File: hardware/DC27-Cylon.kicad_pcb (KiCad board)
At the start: 2 copper layers, 29 parts, among them U1 STM32F030K6Tx, U2 AZ1117-3.3, Y1 16MHz

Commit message: some fixes for fab
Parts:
- added BT1: >VALUE, Sparkfun_Connectors:1X02, F.Cu at (58.4, 63.5)
- C1, C2, C3, C4, C5: footprint Capacitors_SMD:C_0603 -> Sparkfun_Capacitors:0603
- U2: footprint Digikey:SOT-23-3 -> Package_TO_SOT_SMD:SOT-223-3_TabPin2
- moved D1 67.8 mm to (64.8, 78.7), turned to 270 degrees
- moved R1 65.5 mm to (64.8, 74.9), turned to 270 degrees
- moved D2 64.5 mm to (62.2, 78.7), turned to 270 degrees
- moved R2 60.8 mm to (62.2, 74.9), turned to 270 degrees
- moved D3 60.8 mm to (59.7, 78.7), turned to 270 degrees
- moved R4 60.3 mm to (57.1, 74.9), turned to 270 degrees
- moved R6 60.2 mm to (52.1, 74.9), turned to 270 degrees
- moved D7 59.0 mm to (49.5, 78.7), turned to 270 degrees
- moved D9 58.9 mm to (44.5, 78.7), turned to 270 degrees
- moved R3 58.3 mm to (59.7, 74.9), turned to 270 degrees
- moved R5 57.0 mm to (54.6, 74.9), turned to 270 degrees
- moved D8 56.6 mm to (47.0, 78.7), turned to 270 degrees
- moved D6 56.4 mm to (52.1, 78.7), turned to 270 degrees
- moved D4 56.1 mm to (57.1, 78.7), turned to 270 degrees
- moved D5 55.5 mm to (54.6, 78.7), turned to 270 degrees
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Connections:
- net Net-(U1-Pad20) renamed /RX
- net Net-(U1-Pad26) renamed /PB3
- net Net-(U1-Pad27) renamed /PB4
- net Net-(U1-Pad28) renamed /PB5
- R1 pad 1: /PA0 -> /LED0
- R10 pad 1: /PA9 -> /LED9
- R2 pad 1: /PA1 -> /LED1
- R3 pad 1: /PA2 -> /LED2
- R4 pad 1: /PA3 -> /LED3
- R5 pad 1: /PA4 -> /LED4
- R6 pad 1: /PA5 -> /LED5
- R7 pad 1: /PA6 -> /LED6
- R8 pad 1: /PA7 -> /LED7
- R9 pad 1: /PA8 -> /LED8
- U1 pad 10: /PA4 -> /LED5
- U1 pad 11: /PA5 -> /LED4
- U1 pad 12: /PA6 -> /LED3
- U1 pad 13: /PA7 -> /LED2
- U1 pad 14: Net-(U1-Pad14) -> /LED1
- U1 pad 15: Net-(U1-Pad15) -> /LED0
- U1 pad 18: /PA8 -> Net-(U1-Pad18)
- U1 pad 19: /PA9 -> /TX
- U1 pad 31: GND -> Net-(ISP1-Pad3)
- U1 pad 6: /PA0 -> /LED9
- U1 pad 7: /PA1 -> /LED8
- U1 pad 8: /PA2 -> /LED7
- U1 pad 9: /PA3 -> /LED6
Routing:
- net /LED0: track 0.00 -> 28.6 mm
- net /LED1: track 0.00 -> 25.7 mm
- net /LED2: track 0.00 -> 22.9 mm
- net /LED3: track 0.00 -> 20.0 mm
- net +3V3: track 0.00 -> 19.6 mm, vias 0 -> 4
- net /LED4: track 0.00 -> 17.1 mm
- net /RESET: track 0.00 -> 16.4 mm, vias 0 -> 1
- net /LED5: track 0.00 -> 15.2 mm
- net /LED6: track 0.00 -> 13.4 mm
- net /LED7: track 0.00 -> 11.0 mm
- net Net-(ISP1-Pad3): track 0.00 -> 10.7 mm
- net /LED8: track 0.00 -> 10.3 mm
- net /LED9: track 0.00 -> 9.54 mm
- net /O1: track 0.00 -> 9.14 mm
- net Net-(BT1-Pad1): track 0.00 -> 8.66 mm
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- added copper zone on B.Cu, net +3V3
- added copper zone on F.Cu, net GND
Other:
- board outline added: 41.9 x 31.2 mm

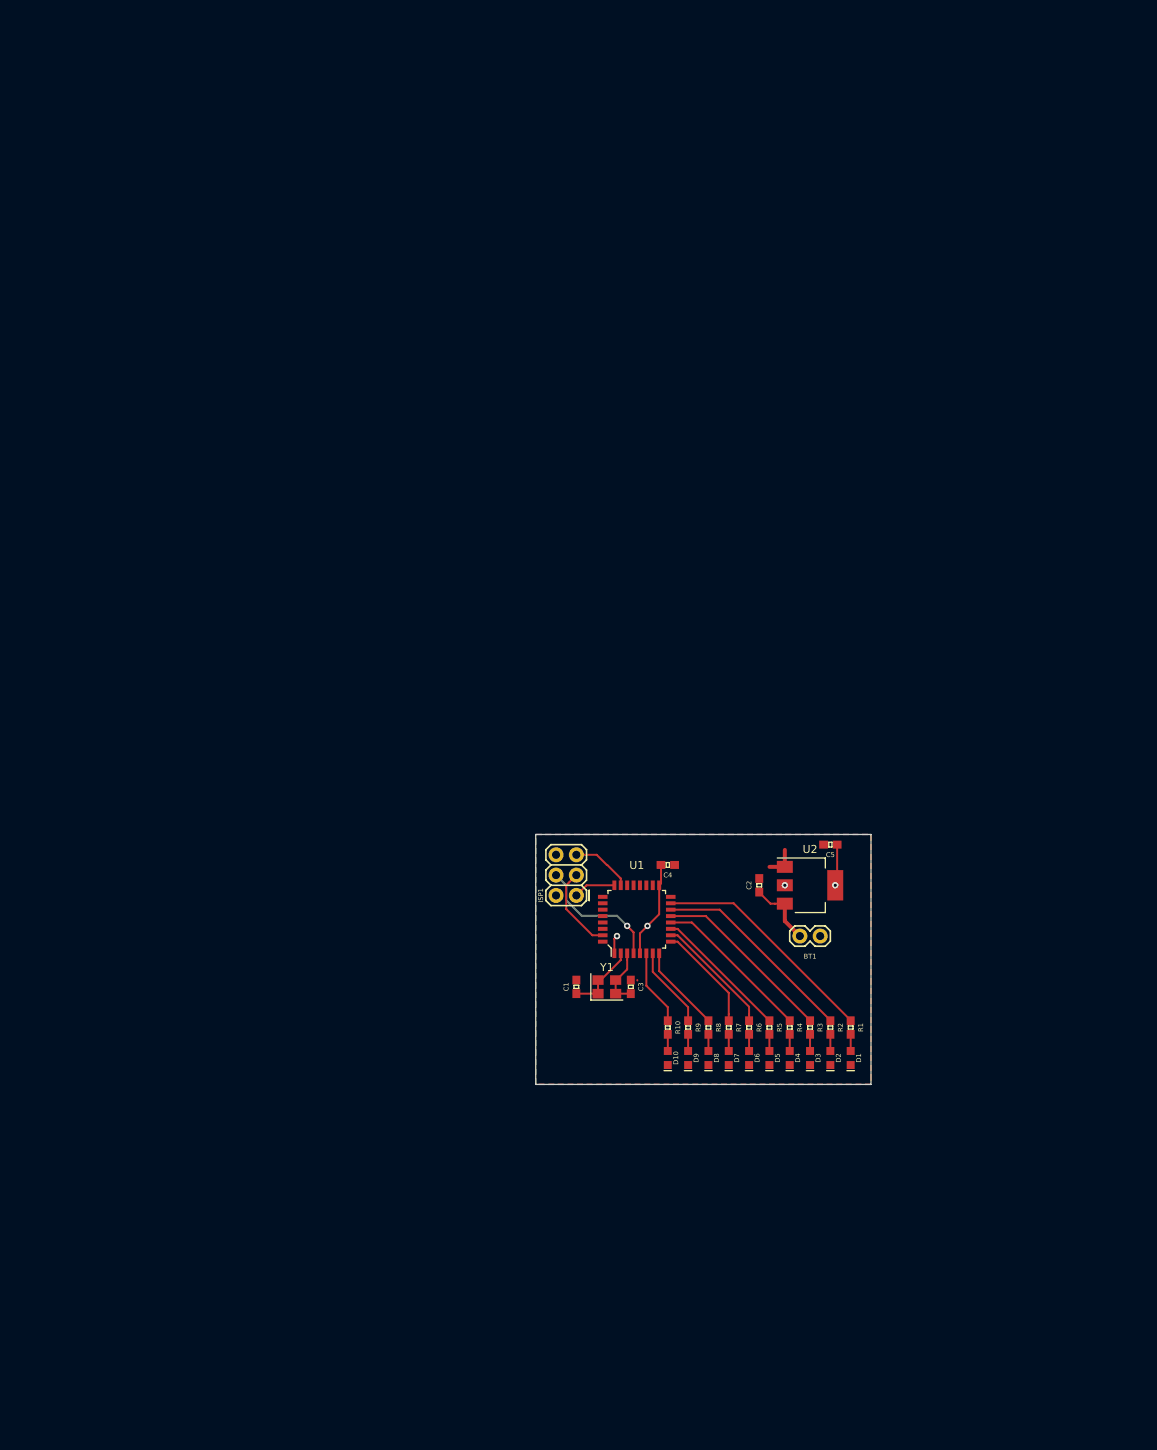
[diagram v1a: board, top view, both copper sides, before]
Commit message: Add board layout to kicad
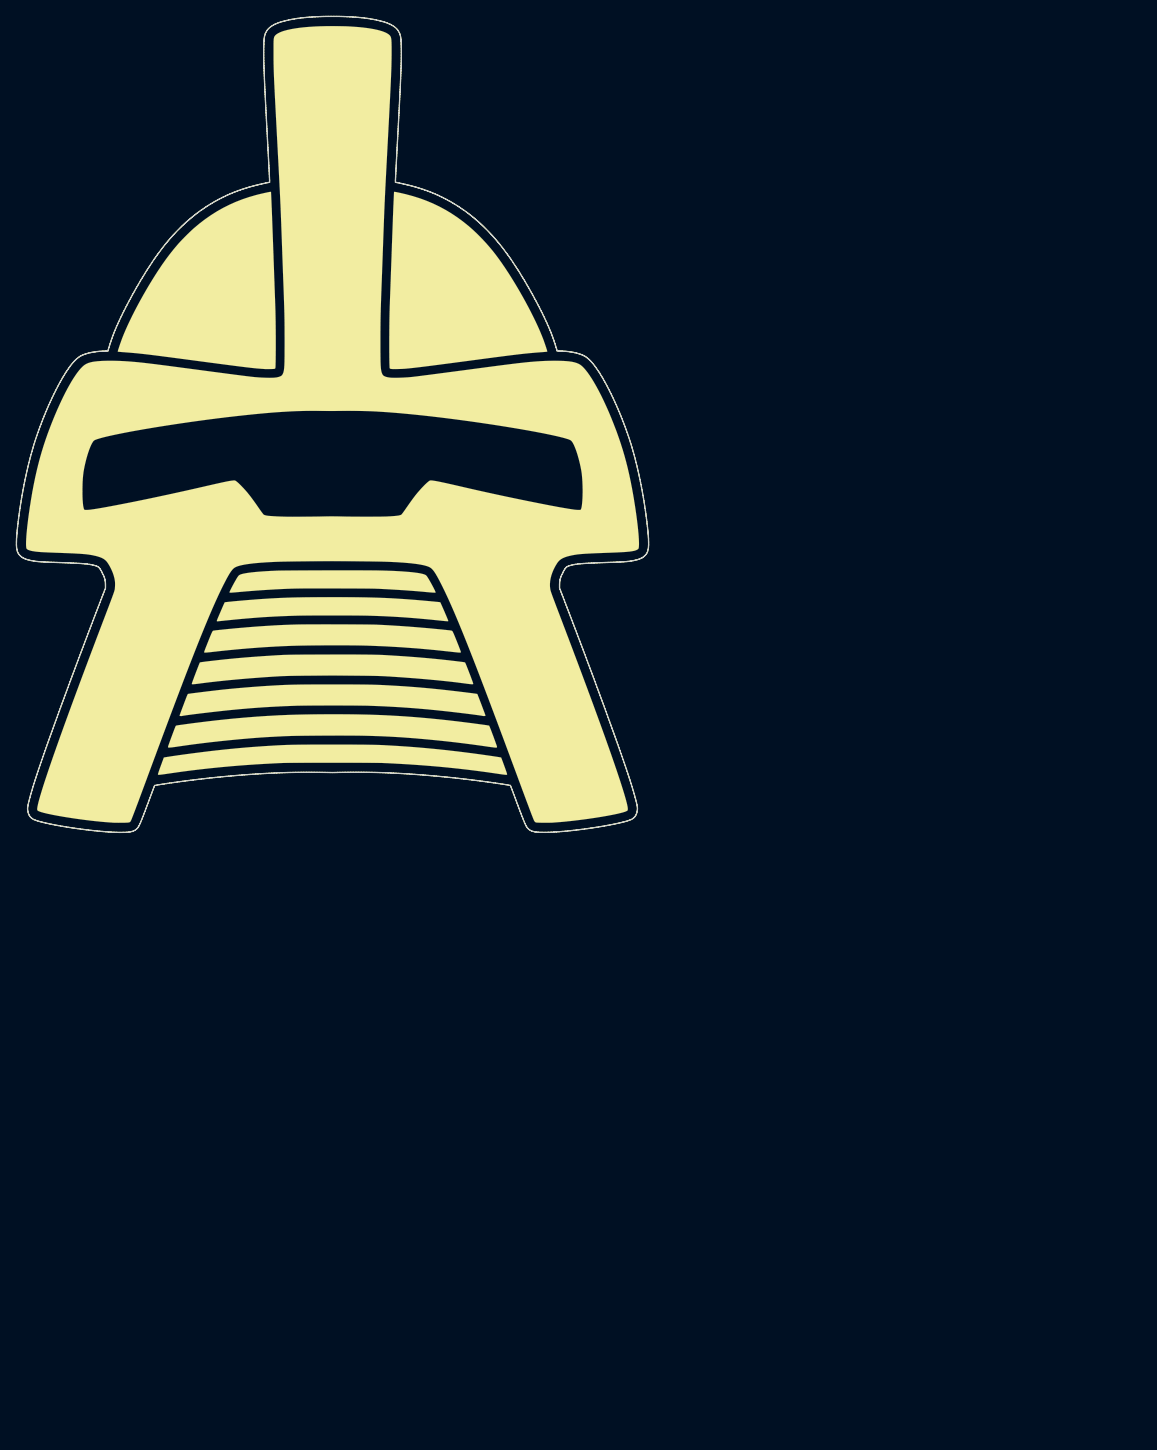
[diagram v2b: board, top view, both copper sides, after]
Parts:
- removed BT1: >VALUE, Sparkfun_Connectors:1X02
- removed C1, C3, C4, C5: 22p, Sparkfun_Capacitors:0603
- removed C2: 10μ, Sparkfun_Capacitors:0603
- removed D1, D10, D2, D3, D4, D5, D6, D7, D8, D9: LED0603, Sparkfun_LED:LED-0603
- removed ISP1: ISP, Sparkfun_Connectors:2X3
- removed R1, R10, R2, R3, R4, R5, R6, R7, R8, R9: 66.3, Sparkfun_Resistors:0603
- removed U1: STM32F030K6Tx, Digikey:LQFP-32_7x7mm
- removed U2: AZ1117-3.3, Package_TO_SOT_SMD:SOT-223-3_TabPin2
- removed Y1: 16MHz, DC27-Cylon:Crystal_SMD_3225-4Pin_3.2x2.5mm
- added G*** (x3): LOGO, LOGO, F.Cu at (0.00, 0.00)
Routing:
- net /LED0: track 28.6 -> 0.00 mm
- net /LED1: track 25.7 -> 0.00 mm
- net /LED2: track 22.9 -> 0.00 mm
- net /LED3: track 20.0 -> 0.00 mm
- net +3V3: track 19.6 -> 0.00 mm, vias 4 -> 0
- net /LED4: track 17.1 -> 0.00 mm
- net /RESET: track 16.4 -> 0.00 mm, vias 1 -> 0
- net /LED5: track 15.2 -> 0.00 mm
- net /LED6: track 13.4 -> 0.00 mm
- net /LED7: track 11.0 -> 0.00 mm
- net Net-(ISP1-Pad3): track 10.7 -> 0.00 mm
- net /LED8: track 10.3 -> 0.00 mm
- net /LED9: track 9.54 -> 0.00 mm
- net /O1: track 9.14 -> 0.00 mm
- net Net-(BT1-Pad1): track 8.66 -> 0.00 mm
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- removed copper zone on B.Cu, net +3V3
- removed copper zone on F.Cu, net GND
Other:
- board size 41.9 x 31.2 mm -> 79 x 102 mm
- net class Default: via_dia 0.8 -> 0.6
- rule pad_to_mask_clearance: 0 -> 0.2

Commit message: Rough layout, still need all tracks
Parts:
- removed the G*** at (0.00, 0.00) (x3)
- added BT1: Battery, DC27-Cylon:BatteryHolder_Keystone_2464_3xAA, B.Cu at (44.2, 58.8)
- added C1: 22p, Sparkfun_Capacitors:0603, B.Cu at (60.7, 99.6)
- added C2: 10μ, Sparkfun_Capacitors:0603, B.Cu at (53.3, 47.0)
- added C3: 22p, Sparkfun_Capacitors:0603, B.Cu at (69.1, 99.8)
- added C4: 22p, Sparkfun_Capacitors:0603, B.Cu at (80.5, 91.9)
- added C5: 22p, Sparkfun_Capacitors:0603, B.Cu at (61.7, 43.2)
- added C6: 22p, Sparkfun_Capacitors:0603, B.Cu at (80.8, 110.7)
- added C7: 22p, Sparkfun_Capacitors:0603, B.Cu at (65.8, 91.9)
- added C8: 22p, Sparkfun_Capacitors:0603, B.Cu at (51.6, 91.9)
- added D1: LED0603, Sparkfun_LED:LED-0603, F.Cu at (80.0, 76.2)
- added D10: LED0603, Sparkfun_LED:LED-0603, F.Cu at (64.0, 76.2)
- added D11: LED0603, Sparkfun_LED:LED-0603, F.Cu at (62.3, 76.2)
- added D12: LED0603, Sparkfun_LED:LED-0603, F.Cu at (60.5, 76.2)
- added D13: LED0603, Sparkfun_LED:LED-0603, F.Cu at (58.7, 76.2)
- added D14: LED0603, Sparkfun_LED:LED-0603, F.Cu at (56.9, 76.2)
- added D15: LED0603, Sparkfun_LED:LED-0603, F.Cu at (55.2, 76.2)
- added D16: LED0603, Sparkfun_LED:LED-0603, F.Cu at (53.4, 76.2)
- added D17: LED0603, Sparkfun_LED:LED-0603, F.Cu at (51.6, 76.2)
- added D18: LED0603, Sparkfun_LED:LED-0603, F.Cu at (49.8, 76.2)
- added D19: LED0603, Sparkfun_LED:LED-0603, F.Cu at (48.1, 76.2)
- added D2: LED0603, Sparkfun_LED:LED-0603, F.Cu at (78.2, 76.2)
- added D20: LED0603, Sparkfun_LED:LED-0603, F.Cu at (46.3, 76.2)
- added D21: LED0603, Sparkfun_LED:LED-0603, F.Cu at (44.5, 76.2)
- added D22: LED0603, Sparkfun_LED:LED-0603, F.Cu at (42.7, 76.2)
- added D23: LED0603, Sparkfun_LED:LED-0603, F.Cu at (41.0, 76.2)
- added D24: LED0603, Sparkfun_LED:LED-0603, F.Cu at (39.2, 76.2)
- added D3: LED0603, Sparkfun_LED:LED-0603, F.Cu at (76.5, 76.2)
- added D4: LED0603, Sparkfun_LED:LED-0603, F.Cu at (74.7, 76.2)
- added D5: LED0603, Sparkfun_LED:LED-0603, F.Cu at (72.9, 76.2)
- added D6: LED0603, Sparkfun_LED:LED-0603, F.Cu at (71.1, 76.2)
- added D7: LED0603, Sparkfun_LED:LED-0603, F.Cu at (69.4, 76.2)
- added D8: LED0603, Sparkfun_LED:LED-0603, F.Cu at (67.6, 76.2)
- added D9: LED0603, Sparkfun_LED:LED-0603, F.Cu at (65.8, 76.2)
- added G***: LOGO, LOGO, F.Cu at (0.00, 0.00)
- added G*** (x2): LOGO, LOGO, F.Cu at (59.4, 73.4)
- added ISP1: ISP, DC27-Cylon:ISP_2X3, B.Cu at (31.5, 110.5)
- added J1: CONN_04LOCK, Sparkfun_Connectors:1X04_LOCK, B.Cu at (93.5, 72.9)
- added J2: CONN_05LOCK, Sparkfun_Connectors:1X05_LOCK, B.Cu at (23.1, 81.8)
- added R1: 66.3, Sparkfun_Resistors:0603, B.Cu at (80.0, 79.4)
- added R10: 66.3, Sparkfun_Resistors:0603, B.Cu at (64.0, 79.4)
- added R11: 66.3, Sparkfun_Resistors:0603, B.Cu at (62.3, 79.4)
- added R12: 66.3, Sparkfun_Resistors:0603, B.Cu at (60.5, 79.4)
- added R13: 66.3, Sparkfun_Resistors:0603, B.Cu at (58.7, 79.4)
- added R14: 66.3, Sparkfun_Resistors:0603, B.Cu at (56.9, 79.4)
- added R15: 66.3, Sparkfun_Resistors:0603, B.Cu at (55.2, 79.4)
- added R16: 66.3, Sparkfun_Resistors:0603, B.Cu at (53.4, 79.4)
- added R17: 66.3, Sparkfun_Resistors:0603, B.Cu at (51.6, 79.4)
- added R18: 66.3, Sparkfun_Resistors:0603, B.Cu at (49.8, 79.4)
- added R19: 66.3, Sparkfun_Resistors:0603, B.Cu at (48.1, 79.4)
- added R2: 66.3, Sparkfun_Resistors:0603, B.Cu at (78.2, 79.4)
- added R20: 66.3, Sparkfun_Resistors:0603, B.Cu at (46.3, 79.4)
- added R21: 66.3, Sparkfun_Resistors:0603, B.Cu at (44.5, 79.4)
- added R22: 66.3, Sparkfun_Resistors:0603, B.Cu at (42.7, 79.4)
- added R23: 66.3, Sparkfun_Resistors:0603, B.Cu at (41.0, 79.4)
- added R24: 66.3, Sparkfun_Resistors:0603, B.Cu at (39.2, 79.4)
- added R3: 66.3, Sparkfun_Resistors:0603, B.Cu at (76.5, 79.4)
- added R4: 66.3, Sparkfun_Resistors:0603, B.Cu at (74.7, 79.4)
- added R5: 66.3, Sparkfun_Resistors:0603, B.Cu at (72.9, 79.4)
- added R6: 66.3, Sparkfun_Resistors:0603, B.Cu at (71.1, 79.4)
- added R7: 66.3, Sparkfun_Resistors:0603, B.Cu at (69.4, 79.4)
- added R8: 66.3, Sparkfun_Resistors:0603, B.Cu at (67.6, 79.4)
- added R9: 66.3, Sparkfun_Resistors:0603, B.Cu at (65.8, 79.4)
- added U1: STM32F030K6Tx, Digikey:LQFP-32_7x7mm, B.Cu at (74.4, 107.2)
- added U2: AZ1117-3.3, Package_TO_SOT_SMD:SOT-223-3_TabPin2, B.Cu at (59.4, 48.3)
- added U3: 74HC595D_118, Digikey:SOIC-16_W3.90mm, B.Cu at (74.4, 91.9)
- added U4: 74HC595D_118, Digikey:SOIC-16_W3.90mm, B.Cu at (59.7, 91.9)
- added U5: 74HC595D_118, Digikey:SOIC-16_W3.90mm, B.Cu at (45.5, 91.9)
- added Y1: 16MHz, DC27-Cylon:Crystal_SMD_3225-4Pin_3.2x2.5mm, B.Cu at (64.5, 100.1)
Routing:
- added copper zone on B.Cu, net +3V3
- added copper zone on F.Cu, net GND
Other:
- outline, holes or cut-outs redrawn

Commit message: Layout all traces
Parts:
- removed the G*** at (59.4, 73.4) (x2)
- added ?: , DC27-Cylon:bazooka_text, B.Cu at (92.1, 110.6)
- added ?: , DC27-Cylon:bazooka, B.Cu at (90.7, 116.7)
- added ?: , DC27-Cylon:p_logo_5_copper, B.Cu at (28.7, 119.8)
- added G*** (x2): LOGO, LOGO, F.Cu at (59.4, 73.4)
- added REF**: Fiducial_0.75mm_Dia_1.5mm_Outer, Fiducials:Fiducial_0.75mm_Dia_1.5mm_Outer, B.Cu at (57.5, 52.1)
- added REF**: Fiducial_0.75mm_Dia_1.5mm_Outer, Fiducials:Fiducial_0.75mm_Dia_1.5mm_Outer, B.Cu at (68.6, 113.2)
- added REF**: Fiducial_0.75mm_Dia_1.5mm_Outer, Fiducials:Fiducial_0.75mm_Dia_1.5mm_Outer, B.Cu at (81.5, 87.5)
- added REF**: Fiducial_0.75mm_Dia_1.5mm_Outer, Fiducials:Fiducial_0.75mm_Dia_1.5mm_Outer, B.Cu at (46.0, 97.3)
- added REF**: Fiducial_0.75mm_Dia_1.5mm_Outer, Fiducials:Fiducial_0.75mm_Dia_1.5mm_Outer, F.Cu at (37.3, 75.7)
- added REF**: Fiducial_0.75mm_Dia_1.5mm_Outer, Fiducials:Fiducial_0.75mm_Dia_1.5mm_Outer, F.Cu at (81.8, 75.7)
- moved C2 18.1 mm to (69.8, 54.4), turned to 0 degrees
- moved C5 10.6 mm to (68.8, 51.1), turned to 90 degrees
- moved U2 5.28 mm to (63.1, 52.1), turned to 180 degrees
- moved C1 5.08 mm to (65.8, 99.4)
- moved Y1 4.24 mm to (68.7, 99.4)
- moved C3 2.58 mm to (71.6, 99.4)
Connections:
- R12 pad 2: Net-(D11-PadA) -> Net-(D12-PadA)
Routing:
- net /PB5: track 0.00 -> 63.2 mm, vias 0 -> 1
- net /PB4: track 0.00 -> 61.5 mm, vias 0 -> 1
- net /PB3: track 0.00 -> 60.0 mm, vias 0 -> 1
- net /TX: track 0.00 -> 59.6 mm
- net /RX: track 0.00 -> 59.0 mm
- net GND: track 0.00 -> 54.1 mm, vias 0 -> 11
- net /RESET: track 0.00 -> 51.7 mm, vias 0 -> 2
- net /SLATCH: track 0.00 -> 44.3 mm, vias 0 -> 3
- net /SCLK: track 0.00 -> 43.5 mm, vias 0 -> 3
- net /SWDIO: track 0.00 -> 43.1 mm
- net /SWCLK: track 0.00 -> 40.5 mm
- net Net-(BT1-Pad1): track 0.00 -> 26.6 mm
- net Net-(U3-Pad9): track 0.00 -> 24.3 mm, vias 0 -> 2
- net Net-(U4-Pad9): track 0.00 -> 23.6 mm, vias 0 -> 2
- net /LED7: track 0.00 -> 15.9 mm
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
